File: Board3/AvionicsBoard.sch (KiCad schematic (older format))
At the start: 69 parts, among them J1 USB_A, J10 I2C, J11 UART, J12 RF IN, J13 RFD900 Connector, J2 Conn_01x02, J3 SWD, J4 7.2V, J5 SPI, J6 Micro_SD_Card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

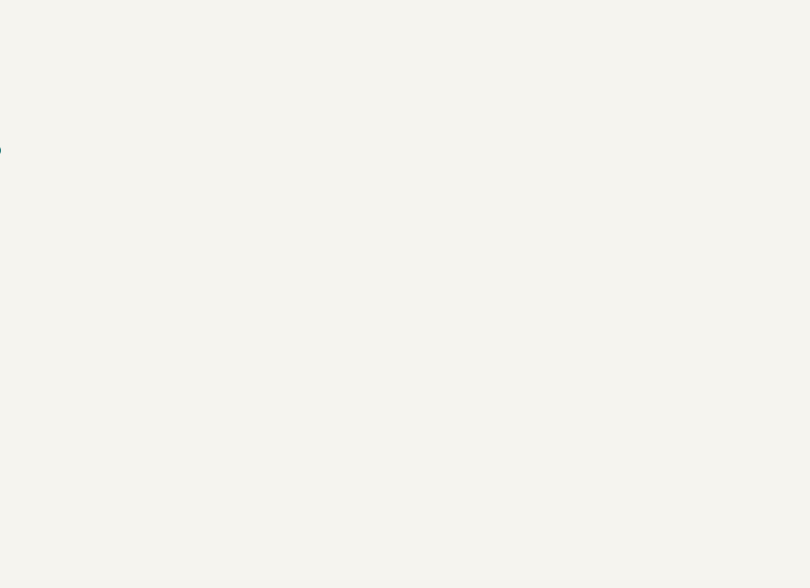
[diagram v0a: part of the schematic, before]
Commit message: Add LEDs, cleanup traces
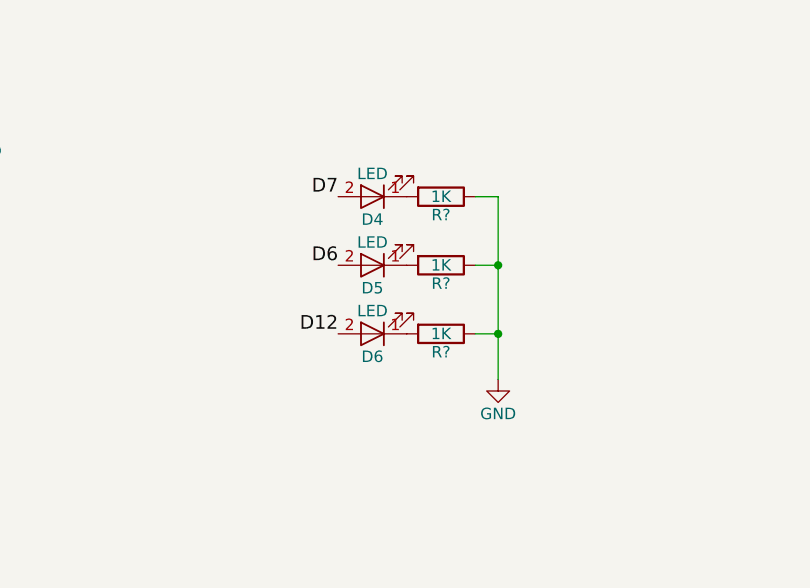
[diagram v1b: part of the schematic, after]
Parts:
- added D4, D5, D6: LED, symbol LED
- added R? (x3): 1K, Resistors_SMD:R_0805, symbol R
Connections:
- wire segments 183 -> 187
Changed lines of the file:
@@
 Text Label 4100 3900 2    60   ~ 0
 D9
-Text Label 4600 3900 0    60   ~ 0
-D10
 $Comp
 L Conn_02x02_Odd_Even J9
@@
 NoConn ~ 10500 2550
 NoConn ~ 10500 2450
+Text Label 4600 3900 0    60   ~ 0
+D10
+$Comp
+L LED D4
+U 1 1 5BDD1B4D
+P 9300 7300
+F 0 "D4" H 9300 7400 50  0000 C CNN
+F 1 "LED" H 9300 7200 50  0000 C CNN
+F 2 "" H 9300 7300 50  0001 C CNN
+F 3 "" H 9300 7300 50  0001 C CNN
+	1    9300 7300
+	-1   0    0    1
+$EndComp
+$Comp
+L LED D5
+U 1 1 5BDD4B11
+P 9300 7600
+F 0 "D5" H 9300 7700 50  0000 C CNN
+F 1 "LED" H 9300 7500 50  0000 C CNN
+F 2 "" H 9300 7600 50  0001 C CNN
+F 3 "" H 9300 7600 50  0001 C CNN
+	1    9300 7600
+	-1   0    0    1
+$EndComp
+$Comp
+L LED D6
+U 1 1 5BDD4BD1
+P 9300 7900
+F 0 "D6" H 9300 8000 50  0000 C CNN
+F 1 "LED" H 9300 7800 50  0000 C CNN
+F 2 "" H 9300 7900 50  0001 C CNN
+F 3 "" H 9300 7900 50  0001 C CNN
+	1    9300 7900
+	-1   0    0    1
+$EndComp
+Text Label 9150 7300 2    60   ~ 0
+D7
+Text Label 9150 7600 2    60   ~ 0
+D6
+Text Label 9150 7900 2    60   ~ 0
+D12
+$Comp
+L GND #PWR082
+U 1 1 5BDD7E94
+P 9850 8100
+F 0 "#PWR082" H 9850 7850 50  0001 C CNN
+F 1 "GND" H 9850 7950 50  0000 C CNN
+F 2 "" H 9850 8100 50  0001 C CNN
+F 3 "" H 9850 8100 50  0001 C CNN
+	1    9850 8100
+	1    0    0    -1
+$EndComp
+Wire Wire Line
+	9850 7300 9850 8100
+Wire Wire Line
+	9850 7900 9750 7900
+Wire Wire Line
+	9850 7600 9750 7600
+Connection ~ 9850 7900
+Wire Wire Line
+	9750 7300 9850 7300
+Connection ~ 9850 7600
+$Comp
+L R R?
+U 1 1 5BDD8D3B
+P 9600 7300
+F 0 "R?" V 9680 7300 50  0000 C CNN
+F 1 "1K" V 9600 7300 50  0000 C CNN
+F 2 "Resistors_SMD:R_0805" V 9530 7300 50  0001 C CNN
+F 3 "" H 9600 7300 50  0001 C CNN
+	1    9600 7300
+	0    1    1    0
+$EndComp
+$Comp
+L R R?
+U 1 1 5BDD91DC
+P 9600 7600
+F 0 "R?" V 9680 7600 50  0000 C CNN
+F 1 "1K" V 9600 7600 50  0000 C CNN
+F 2 "Resistors_SMD:R_0805" V 9530 7600 50  0001 C CNN
+F 3 "" H 9600 7600 50  0001 C CNN
+	1    9600 7600
+	0    1    1    0
+$EndComp
+$Comp
+L R R?
+U 1 1 5BDD92DE
+P 9600 7900
+F 0 "R?" V 9680 7900 50  0000 C CNN
+F 1 "1K" V 9600 7900 50  0000 C CNN
+F 2 "Resistors_SMD:R_0805" V 9530 7900 50  0001 C CNN
+F 3 "" H 9600 7900 50  0001 C CNN
+	1    9600 7900
+	0    1    1    0
+$EndComp
 $EndSCHEMATC

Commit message: Doen
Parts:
- D4, D5, D6: footprint (none) -> LEDs:LED_1206
- J12, J7: footprint Connectors:SMA_SMD_Jack_Straight -> FoxWestern:SMA_TH
- gave numbers to parts that had none: 3
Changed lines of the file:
@@
 F 0 "J7" H 7810 1870 50  0000 C CNN
 F 1 "RF IN" V 7915 1750 50  0000 C CNN
-F 2 "Connectors:SMA_SMD_Jack_Straight" H 7800 1750 50  0001 C CNN
+F 2 "FoxWestern:SMA_TH" H 7800 1750 50  0001 C CNN
 F 3 "" H 7800 1750 50  0001 C CNN
 	1    7800 1750
@@
 F 0 "J12" H 3660 10670 50  0000 C CNN
 F 1 "RF IN" V 3765 10550 50  0000 C CNN
-F 2 "Connectors:SMA_SMD_Jack_Straight" H 3650 10550 50  0001 C CNN
+F 2 "FoxWestern:SMA_TH" H 3650 10550 50  0001 C CNN
 F 3 "" H 3650 10550 50  0001 C CNN
 	1    3650 10550
@@
 F 0 "D4" H 9300 7400 50  0000 C CNN
 F 1 "LED" H 9300 7200 50  0000 C CNN
-F 2 "" H 9300 7300 50  0001 C CNN
+F 2 "LEDs:LED_1206" H 9300 7300 50  0001 C CNN
 F 3 "" H 9300 7300 50  0001 C CNN
 	1    9300 7300
@@
 F 0 "D5" H 9300 7700 50  0000 C CNN
 F 1 "LED" H 9300 7500 50  0000 C CNN
-F 2 "" H 9300 7600 50  0001 C CNN
+F 2 "LEDs:LED_1206" H 9300 7600 50  0001 C CNN
 F 3 "" H 9300 7600 50  0001 C CNN
 	1    9300 7600
@@
 F 0 "D6" H 9300 8000 50  0000 C CNN
 F 1 "LED" H 9300 7800 50  0000 C CNN
-F 2 "" H 9300 7900 50  0001 C CNN
+F 2 "LEDs:LED_1206" H 9300 7900 50  0001 C CNN
 F 3 "" H 9300 7900 50  0001 C CNN
 	1    9300 7900
@@
 Connection ~ 9850 7600
 $Comp
-L R R?
+L R R19
 U 1 1 5BDD8D3B
 P 9600 7300
-F 0 "R?" V 9680 7300 50  0000 C CNN
+F 0 "R19" V 9680 7300 50  0000 C CNN
 F 1 "1K" V 9600 7300 50  0000 C CNN
 F 2 "Resistors_SMD:R_0805" V 9530 7300 50  0001 C CNN
@@
 $EndComp
 $Comp
-L R R?
+L R R20
 U 1 1 5BDD91DC
 P 9600 7600
-F 0 "R?" V 9680 7600 50  0000 C CNN
+F 0 "R20" V 9680 7600 50  0000 C CNN
 F 1 "1K" V 9600 7600 50  0000 C CNN
 F 2 "Resistors_SMD:R_0805" V 9530 7600 50  0001 C CNN
@@
 $EndComp
 $Comp
-L R R?
+L R R21
 U 1 1 5BDD92DE
 P 9600 7900
-F 0 "R?" V 9680 7900 50  0000 C CNN
+F 0 "R21" V 9680 7900 50  0000 C CNN
 F 1 "1K" V 9600 7900 50  0000 C CNN
 F 2 "Resistors_SMD:R_0805" V 9530 7900 50  0001 C CNN
